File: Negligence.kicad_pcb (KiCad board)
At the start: 2 copper layers, 112 parts, among them J1 AVR-ISP-6, SW1 keyboard_parts_KEYSW, SW10 keyboard_parts_KEYSW, SW11 keyboard_parts_KEYSW, SW12 keyboard_parts_KEYSW, SW13 keyboard_parts_KEYSW, SW14 keyboard_parts_KEYSW, SW15 keyboard_parts_KEYSW, SW16 keyboard_parts_KEYSW, SW17 keyboard_parts_KEYSW, SW18 keyboard_parts_KEYSW, SW19 keyboard_parts_KEYSW, SW2 keyboard_parts_KEYSW, SW20 keyboard_parts_KEYSW, SW21 keyboard_parts_KEYSW, SW22 keyboard_parts_KEYSW, SW23 keyboard_parts_KEYSW, SW24 keyboard_parts_KEYSW, SW25 keyboard_parts_KEYSW, SW26 keyboard_parts_KEYSW, SW27 keyboard_parts_KEYSW, SW28 keyboard_parts_KEYSW, SW29 keyboard_parts_KEYSW, SW3 keyboard_parts_KEYSW, SW30 keyboard_parts_KEYSW, SW31 keyboard_parts_KEYSW, SW32 keyboard_parts_KEYSW, SW33 keyboard_parts_KEYSW, SW34 keyboard_parts_KEYSW, SW35 keyboard_parts_KEYSW, SW36 keyboard_parts_KEYSW, SW37 keyboard_parts_KEYSW, SW38 keyboard_parts_KEYSW, SW39 keyboard_parts_KEYSW, SW4 keyboard_parts_KEYSW, SW40 keyboard_parts_KEYSW, SW41 keyboard_parts_KEYSW, SW42 keyboard_parts_KEYSW, SW43 keyboard_parts_KEYSW, SW44 keyboard_parts_KEYSW, SW45 keyboard_parts_KEYSW, SW46 keyboard_parts_KEYSW, SW47 RESET, SW48 BOOT, SW5 keyboard_parts_KEYSW, SW6 keyboard_parts_KEYSW, SW7 keyboard_parts_KEYSW, SW8 keyboard_parts_KEYSW, SW9 keyboard_parts_KEYSW, U1 ATmega328P-PU, Y1 16MHz

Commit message: Start wiring switches
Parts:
- moved D3 229.3 mm to (48.3, 61.0), turned to 270 degrees
- moved D1 221.8 mm to (22.9, 61.0), turned to 270 degrees
- moved D4 220.1 mm to (70.1, 64.8), turned to 270 degrees
- moved D2 216.9 mm to (45.1, 64.8), turned to 270 degrees
- moved D44 197.0 mm to (132.5, 64.3), turned to 270 degrees
- moved D7 196.2 mm to (110.2, 60.5), turned to 270 degrees
- moved D8 163.0 mm to (122.9, 60.5), turned to 270 degrees
- moved D13 132.0 mm to (26.0, 62.2), turned to 270 degrees
- moved D35 120.0 mm to (167.4, 63.0), turned to 270 degrees
- moved D25 118.8 mm to (29.2, 63.5), turned to 270 degrees
- moved D46 112.6 mm to (157.9, 64.3), turned to 270 degrees
- moved D34 112.2 mm to (154.7, 63.0), turned to 270 degrees
- moved D23 108.9 mm to (164.2, 61.7), turned to 270 degrees
- moved D33 108.3 mm to (142.0, 63.0), turned to 270 degrees
- moved D43 104.9 mm to (119.8, 64.3), turned to 270 degrees
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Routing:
- net Net-(D41-Pad2): track 0.00 -> 97.4 mm
- net Net-(D39-Pad2): track 0.00 -> 87.7 mm
- net Net-(D40-Pad2): track 0.00 -> 87.4 mm
- net Net-(D29-Pad2): track 0.00 -> 85.0 mm
- net Net-(D38-Pad2): track 0.00 -> 82.5 mm
- net Net-(D37-Pad2): track 0.00 -> 81.4 mm
- net Net-(D27-Pad2): track 0.00 -> 71.2 mm
- net Net-(D17-Pad2): track 0.00 -> 68.4 mm
- net Net-(D25-Pad2): track 0.00 -> 65.4 mm
- net Net-(D28-Pad2): track 0.00 -> 65.0 mm
- net Net-(D26-Pad2): track 0.00 -> 60.1 mm
- net Net-(D15-Pad2): track 0.00 -> 54.6 mm
- net Net-(D5-Pad2): track 0.00 -> 53.3 mm
- net Net-(D13-Pad2): track 0.00 -> 48.9 mm
- net Net-(D30-Pad2): track 0.00 -> 43.7 mm
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
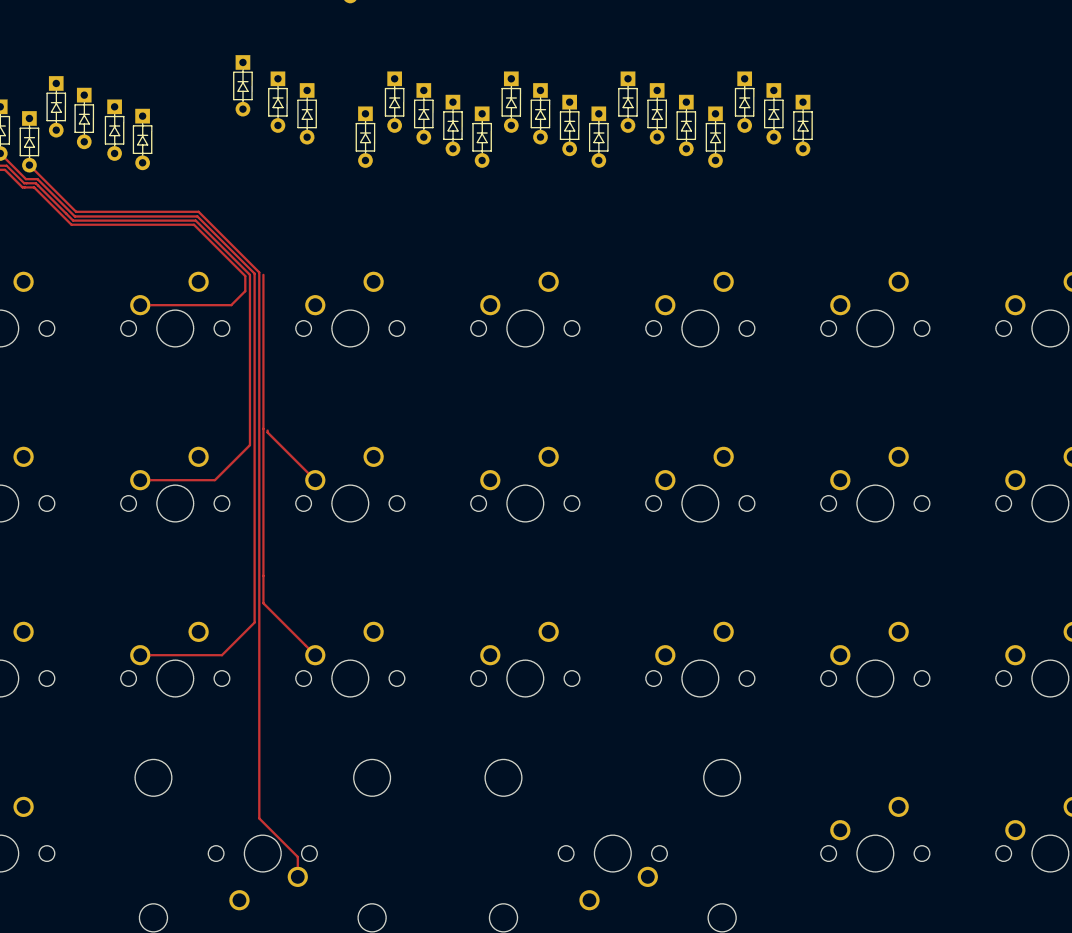
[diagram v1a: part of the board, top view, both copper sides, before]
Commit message: More key sw traces
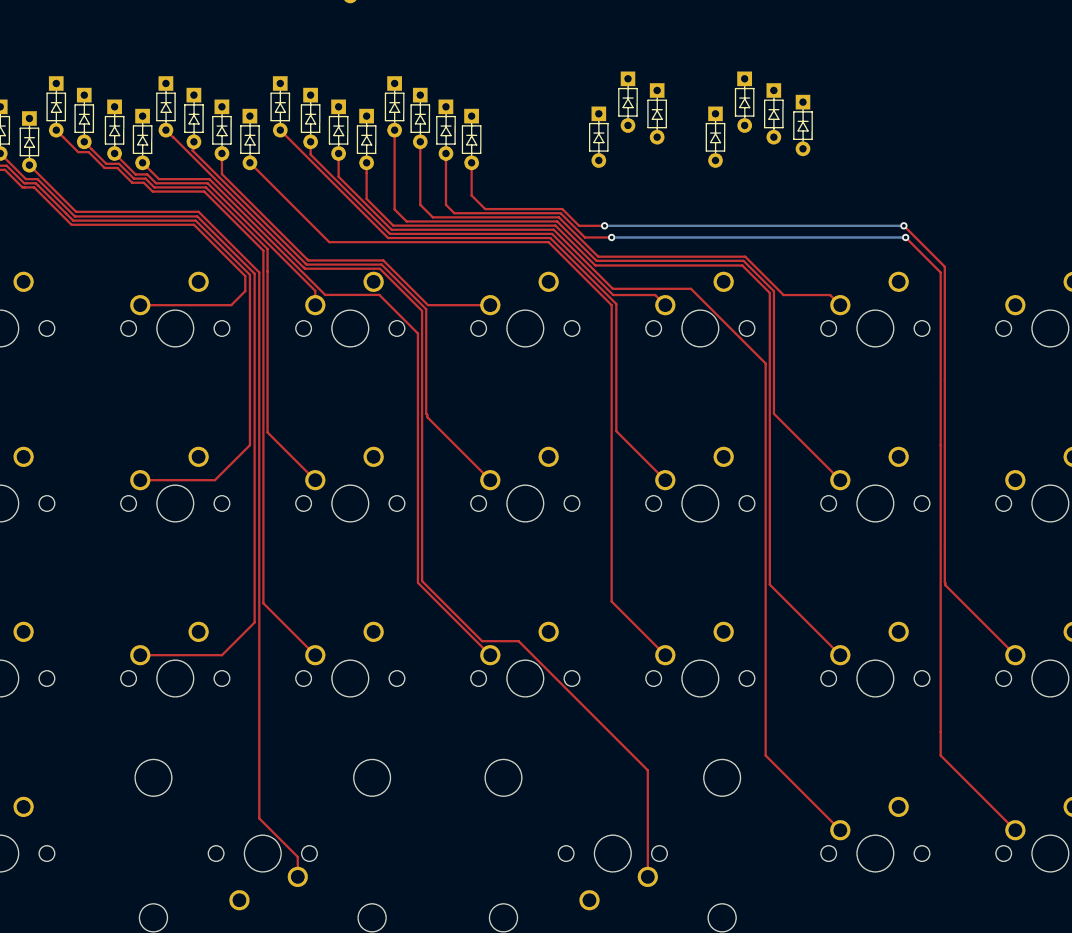
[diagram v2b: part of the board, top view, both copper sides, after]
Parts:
- moved D34 23.4 mm to (131.3, 64.5)
- moved D32 22.2 mm to (107.2, 64.5)
- moved D33 22.2 mm to (119.9, 64.5)
- moved D21 15.9 mm to (122.9, 61.0)
- moved D20 15.6 mm to (110.5, 61.0)
- moved D19 12.3 mm to (101.1, 62.2)
- moved D9 10.1 mm to (125.7, 62.2)
- moved D8 9.32 mm to (113.8, 62.2)
- moved D42 8.69 mm to (98.0, 61.0)
- moved D7 6.82 mm to (104.1, 63.5)
- moved D44 4.01 mm to (128.5, 63.5)
- moved D43 3.02 mm to (116.8, 63.5)
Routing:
- net Net-(D44-Pad2): track 0.00 -> 126.6 mm, vias 0 -> 2
- net Net-(D43-Pad2): track 0.00 -> 111.6 mm
- net Net-(D42-Pad2): track 0.00 -> 110.1 mm
- net Net-(D34-Pad2): track 0.00 -> 103.7 mm, vias 0 -> 2
- net Net-(D33-Pad2): track 0.00 -> 94.7 mm
- net Net-(D32-Pad2): track 0.00 -> 86.3 mm
- net Net-(D21-Pad2): track 0.00 -> 77.2 mm
- net Net-(D31-Pad2): track 0.00 -> 75.9 mm
- net Net-(D20-Pad2): track 0.00 -> 65.8 mm
- net Net-(D9-Pad2): track 0.00 -> 57.1 mm
- net Net-(D19-Pad2): track 0.00 -> 55.1 mm
- net Net-(D8-Pad2): track 0.00 -> 46.8 mm
- net Net-(D18-Pad2): track 7.55 -> 52.1 mm
- net Net-(D7-Pad2): track 0.00 -> 37.4 mm
- net Net-(D30-Pad2): track 43.7 -> 74.4 mm
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
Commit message: Finish diode wiring
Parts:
- moved U1 270.0 mm to (193.3, 69.6), turned to 90 degrees
- moved D36 85.6 mm to (156.5, 62.2)
- moved D24 73.3 mm to (159.5, 63.5)
- moved D12 69.1 mm to (162.6, 64.5)
- moved D35 23.2 mm to (144.3, 64.5)
- moved D23 17.0 mm to (147.3, 63.5)
- moved D22 16.4 mm to (135.1, 61.0)
- moved D11 10.8 mm to (150.4, 62.2)
- moved D10 10.3 mm to (138.2, 62.2)
- moved D46 5.54 mm to (153.4, 61.0)
- moved D45 4.01 mm to (141.2, 63.5)
- moved D34 0.76 mm to (132.1, 64.5)
- moved D44 0.51 mm to (129.0, 63.5)
- moved D9 0.25 mm to (126.0, 62.2)
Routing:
- net Net-(D46-Pad2): track 0.00 -> 139.5 mm
- net Net-(D45-Pad2): track 0.00 -> 130.0 mm
- net Net-(D36-Pad2): track 0.00 -> 116.2 mm
- net Net-(D35-Pad2): track 0.00 -> 109.0 mm
- net Net-(D24-Pad2): track 0.00 -> 93.0 mm
- net Net-(D23-Pad2): track 0.00 -> 87.6 mm
- net Net-(D22-Pad2): track 0.00 -> 84.5 mm
- net Net-(D12-Pad2): track 0.00 -> 74.3 mm
- net Net-(D11-Pad2): track 0.00 -> 70.1 mm
- net Net-(D10-Pad2): track 0.00 -> 62.5 mm
- net Net-(D21-Pad2): track 77.2 -> 72.9 mm
- net Net-(D9-Pad2): track 57.1 -> 54.3 mm
- net Net-(D44-Pad2): track 126.6 -> 124.2 mm, vias 2 -> 0
- net Net-(D34-Pad2): track 103.7 -> 102.6 mm, vias 2 -> 0

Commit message: Space saving
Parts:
- moved U1 36.2 mm to (228.9, 63.0), turned to 270 degrees

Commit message: Start MCU wiring
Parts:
- added REF**: MountingHole_2.2mm_M2_Pad, cftkb:MountingHole_2.2mm_M2_Pad, F.Cu at (16.8, 75.4)
- added REF**: MountingHole_2.2mm_M2_Pad, cftkb:MountingHole_2.2mm_M2_Pad, F.Cu at (16.8, 59.4)
- added REF**: MountingHole_2.2mm_M2_Pad, cftkb:MountingHole_2.2mm_M2_Pad, F.Cu at (238.3, 75.4)
- added REF**: MountingHole_2.2mm_M2_Pad, cftkb:MountingHole_2.2mm_M2_Pad, F.Cu at (238.3, 59.4)
- moved SW47 167.7 mm to (214.5, 41.9)
- moved U1 1.61 mm to (230.4, 63.5)
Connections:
- net /MISO renamed Net-(J1-Pad1)
- net /MOSI renamed Net-(J1-Pad4)
- J1 pad 3: /SCK -> /COL2
- U1 pad 19: /SCK -> /COL2
- U1 pad 2: Net-(U1-Pad2) -> /COL11
- U1 pad 23: Net-(U1-Pad23) -> /COL8
- U1 pad 24: Net-(U1-Pad24) -> /COL7
- U1 pad 25: Net-(U1-Pad25) -> /COL6
- U1 pad 26: Net-(U1-Pad26) -> /COL5
- U1 pad 27: Net-(U1-Pad27) -> /COL4
- U1 pad 28: Net-(U1-Pad28) -> /COL3
- U1 pad 3: Net-(U1-Pad3) -> /COL10
- U1 pad 4: Net-(U1-Pad4) -> /D+
- U1 pad 5: Net-(U1-Pad5) -> /D-
- U1 pad 6: Net-(U1-Pad6) -> /COL9
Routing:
- net /COL6: track 0.00 -> 121.5 mm
- net /COL4: track 0.00 -> 107.2 mm
- net /COL7: track 0.00 -> 106.8 mm
- net /COL8: track 0.00 -> 91.8 mm
- net /COL9: track 0.00 -> 76.5 mm
- net /COL10: track 0.00 -> 50.1 mm
- net /COL11: track 0.00 -> 30.6 mm
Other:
- board outline added: 228.9 x 100.3 mm

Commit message: Finish mcu
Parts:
- moved J1 237.3 mm to (192.5, 59.2), turned to 180 degrees
- moved SW48 146.6 mm to (166.1, 58.2)
- moved F1 127.5 mm to (106.3, -4.33)
- moved SW47 40.2 mm to (177.8, 58.2)
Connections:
- J1 pad 1: Net-(J1-Pad1) -> /COL1
- J1 pad 4: Net-(J1-Pad4) -> /COL0
- U1 pad 17: Net-(J1-Pad4) -> /COL0
- U1 pad 18: Net-(J1-Pad1) -> /COL1
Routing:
- net /COL0: track 0.00 -> 261.4 mm, vias 0 -> 2
- net /COL1: track 0.00 -> 247.2 mm, vias 0 -> 1
- net /COL2: track 0.00 -> 236.5 mm, vias 0 -> 2
- net /COL3: track 0.00 -> 215.9 mm
- net /COL5: track 0.00 -> 174.0 mm
- net /COL4: track 107.2 -> 217.4 mm
- net /COL6: track 121.5 -> 191.1 mm
- net /COL8: track 91.8 -> 149.4 mm
- net /COL11: track 30.6 -> 87.8 mm
- net /COL10: track 50.1 -> 107.3 mm
- net /COL9: track 76.5 -> 133.6 mm
- net Net-(SW48-Pad1): track 0.00 -> 41.4 mm
- net /COL7: track 106.8 -> 145.4 mm
- net +5V: track 0.00 -> 21.8 mm, vias 0 -> 1
- net /RESET: track 0.00 -> 12.3 mm

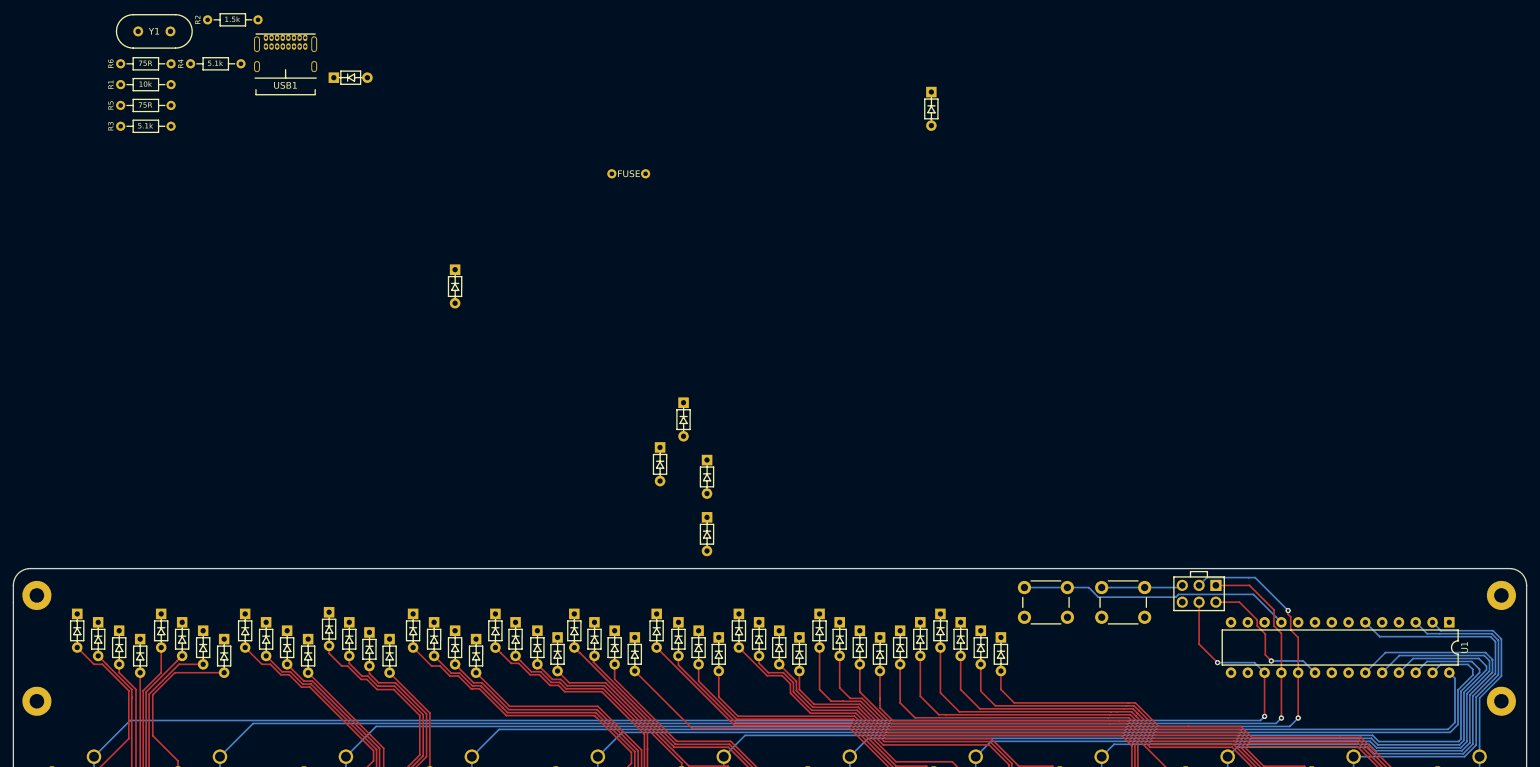
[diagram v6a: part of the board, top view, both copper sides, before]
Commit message: Edge cuts and place components on board
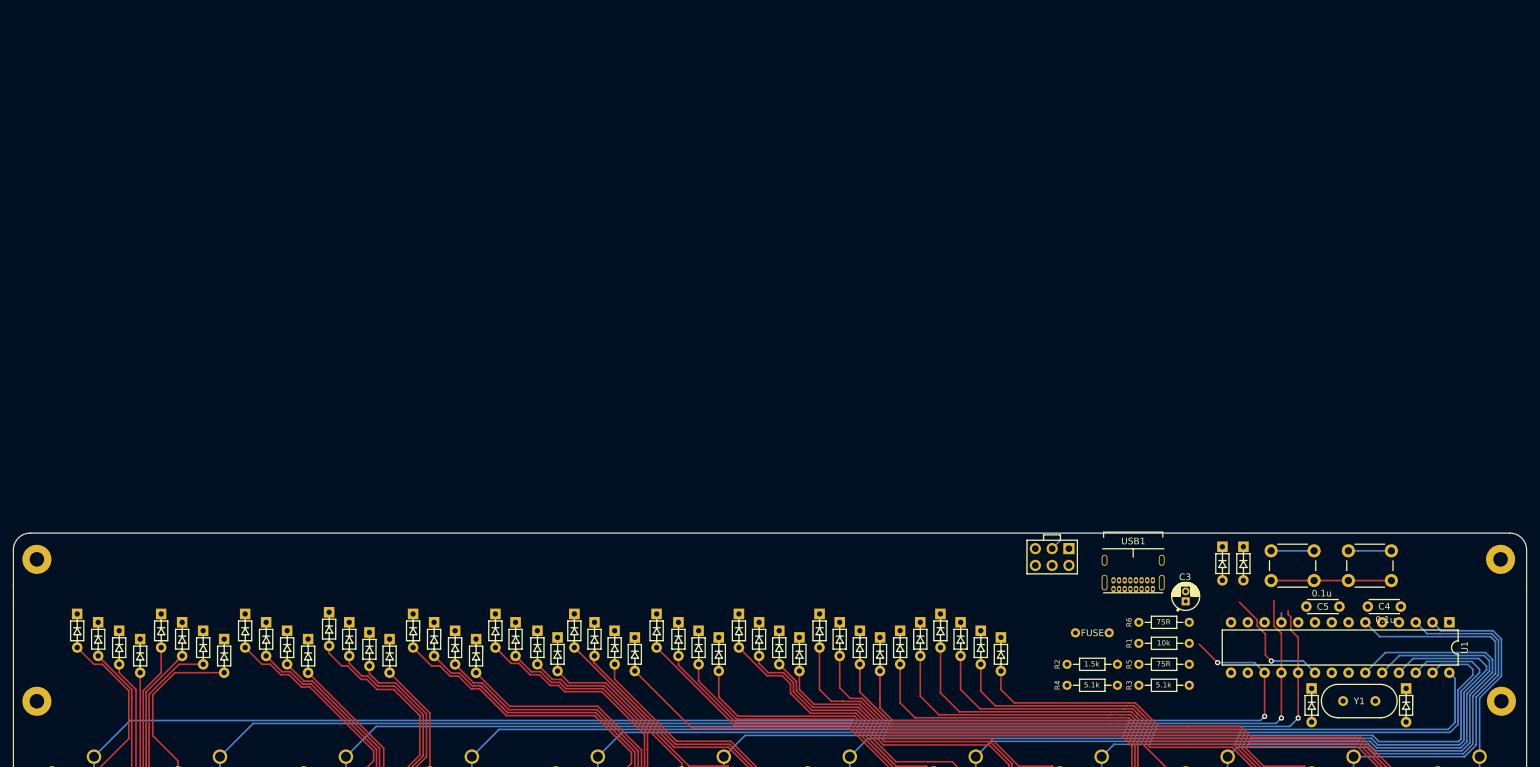
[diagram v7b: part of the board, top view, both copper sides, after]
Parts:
- C3: footprint cftkb:D_DO-35_SOD27_P5.08mm_Horizontal -> cftkb:CP_Radial_D4.0mm_P1.50mm
- C4, C5: footprint cftkb:D_DO-35_SOD27_P5.08mm_Horizontal -> cftkb:C_Disc_D4.3mm_W1.9mm_P5.00mm
- moved Y1 208.5 mm to (214.3, 75.4)
- moved R3 175.7 mm to (183.4, 73.0)
- moved R5 175.7 mm to (183.4, 69.8)
- moved R1 175.6 mm to (183.4, 66.7)
- moved R6 175.6 mm to (183.4, 63.5)
- moved R4 162.5 mm to (172.6, 73.0)
- moved R2 162.5 mm to (172.6, 69.8)
- moved D48 155.3 mm to (199.2, 50.8), turned to 270 degrees
- moved USB1 146.6 mm to (182.6, 52.4), turned to 180 degrees
- moved D47 123.4 mm to (196.1, 50.8)
- moved C1 108.8 mm to (223.8, 72.2)
- moved C2 105.1 mm to (209.6, 72.2)
- moved C4 102.6 mm to (218.0, 61.1), turned to 0 degrees
- moved C5 100.3 mm to (213.8, 61.1), turned to 180 degrees
- moved F1 98.7 mm to (176.4, 65.1)
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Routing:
- net Net-(SW48-Pad1): track 41.4 -> 7.90 mm
- net GND: track 0.00 -> 18.2 mm
- net /COL2: track 236.5 -> 222.1 mm, vias 2 -> 1
- net /COL1: track 247.2 -> 238.4 mm
- net /COL0: track 261.4 -> 255.0 mm
- net /RESET: track 12.3 -> 6.50 mm
- net +5V: track 21.8 -> 18.2 mm
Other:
- board size 228.9 x 100.3 mm -> 228.9 x 105.7 mm

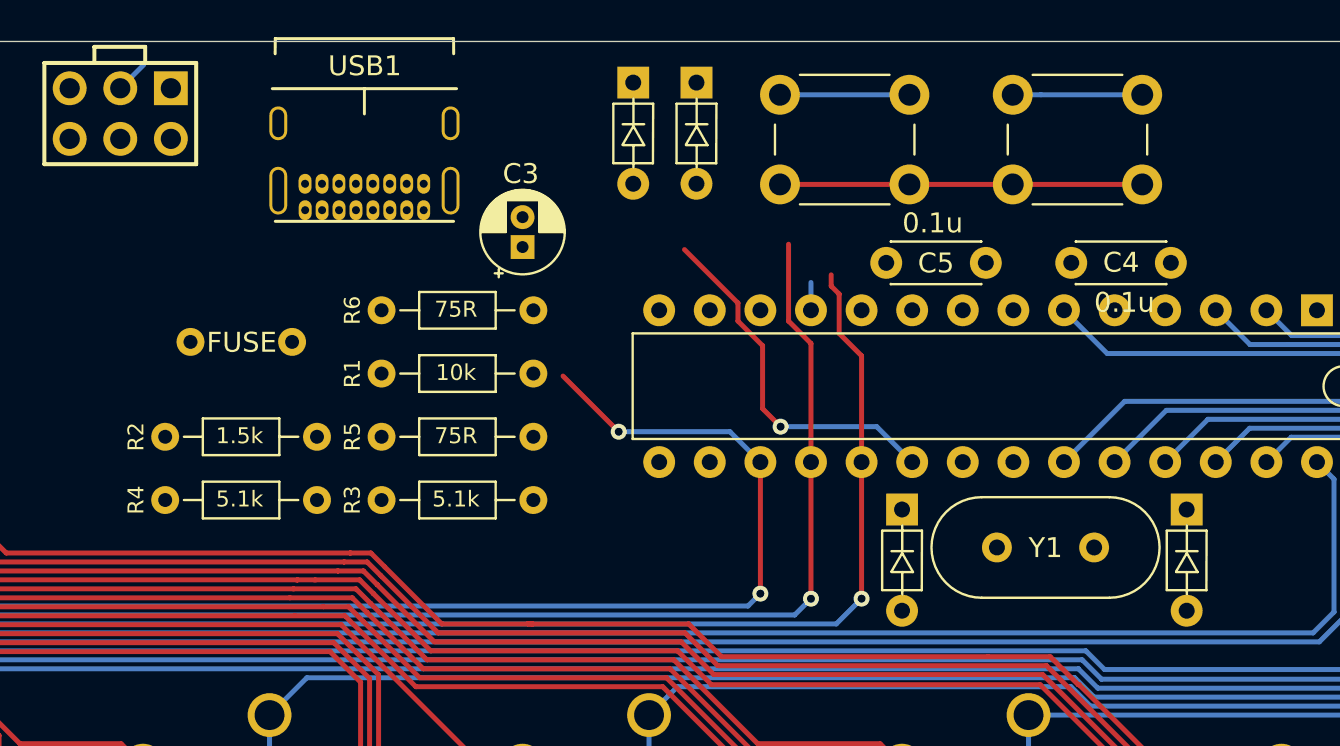
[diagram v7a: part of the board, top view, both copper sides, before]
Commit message: Wire USB, various
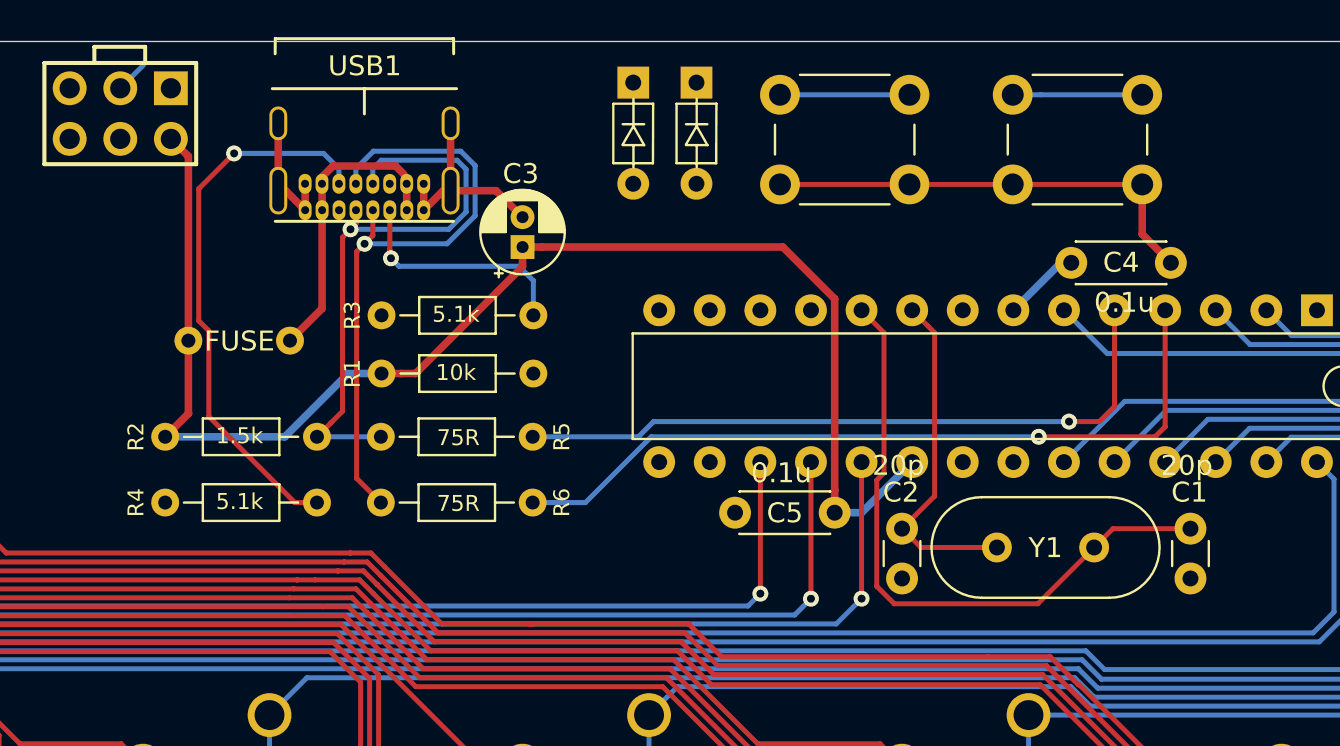
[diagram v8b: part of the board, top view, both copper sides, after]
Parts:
- C1, C2: footprint cftkb:D_DO-35_SOD27_P5.08mm_Horizontal -> cftkb:C_Disc_D3.0mm_W1.6mm_P2.50mm
- moved C5 14.7 mm to (206.2, 73.7)
- moved R6 12.3 mm to (191.0, 73.2), turned to 180 degrees
- moved R3 9.27 mm to (183.4, 63.8)
- moved R5 7.59 mm to (191.0, 69.8), turned to 180 degrees
- moved C1 2.24 mm to (224.0, 74.5)
- moved C2 2.23 mm to (209.6, 74.5)
- moved R4 0.13 mm to (172.6, 73.2)
- moved F1 0.12 mm to (176.3, 65.0)
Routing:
- net +5V: track 18.2 -> 74.6 mm, vias 1 -> 0
- net /D+: track 0.00 -> 39.4 mm, vias 0 -> 1
- net /D-: track 0.00 -> 34.7 mm, vias 0 -> 1
- net Net-(C1-Pad1): track 0.00 -> 32.1 mm
- net Net-(D48-Pad1): track 0.00 -> 31.6 mm, vias 0 -> 1
- net Net-(D47-Pad1): track 0.00 -> 29.5 mm, vias 0 -> 1
- net Net-(R4-Pad2): track 0.00 -> 27.7 mm, vias 0 -> 1
- net GND: track 18.2 -> 39.8 mm
- net Net-(C2-Pad1): track 0.00 -> 17.3 mm
- net VCC: track 0.00 -> 14.7 mm
- net Net-(R3-Pad2): track 0.00 -> 11.8 mm, vias 0 -> 1
- net /COL0: track 255.0 -> 243.3 mm, vias 2 -> 1
- net /COL1: track 238.4 -> 227.0 mm
- net /COL2: track 222.1 -> 212.1 mm
- net Net-(SW48-Pad1): track 7.90 -> 6.50 mm
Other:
- net class Default: trace_width 0.25 -> 0.254
- net class Power added: clearance 0.2, trace_width 0.381, via_dia 0.8, via_drill 0.4
